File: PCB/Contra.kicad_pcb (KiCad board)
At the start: 2 copper layers, 251.5 x 76.2 mm, 152 parts, among them J1 Conn_01x03, J2 Conn_01x02, SW1 SW_PUSH, SW2 SW_SPDT, U1 ProMicro

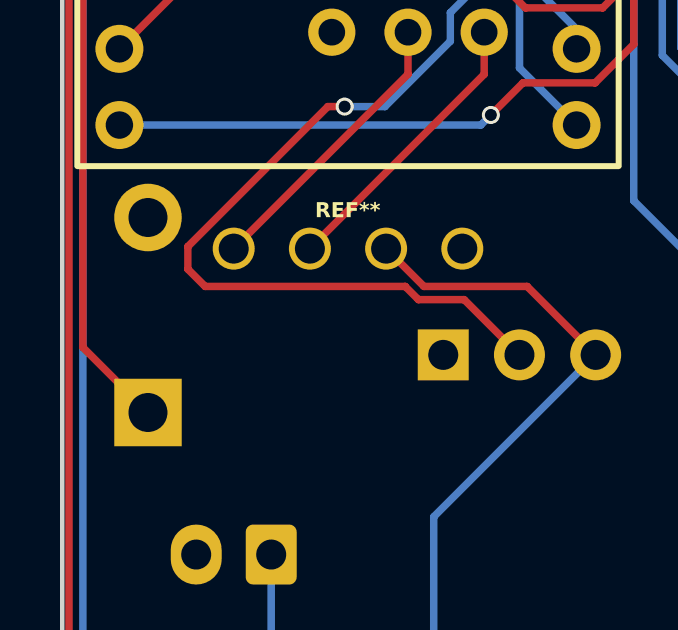
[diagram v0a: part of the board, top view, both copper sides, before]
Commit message: tweak reset switch location
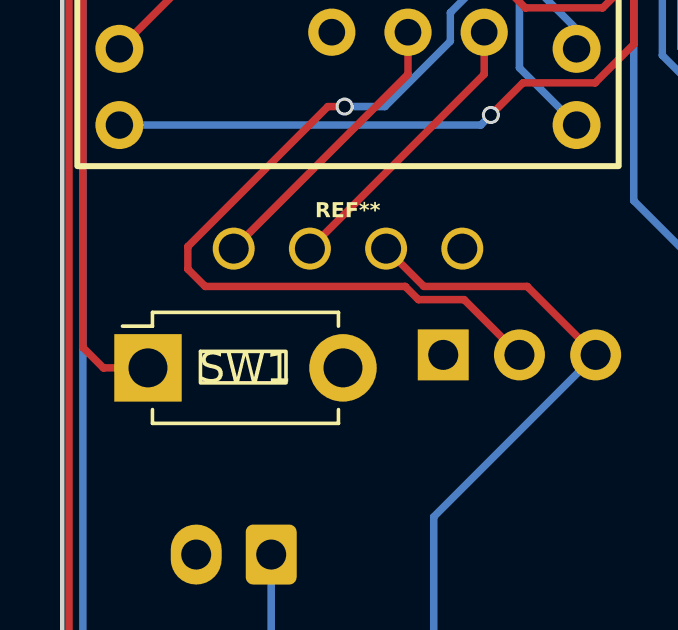
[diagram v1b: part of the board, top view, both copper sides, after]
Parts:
- SW1: moved to F.Cu
- moved SW1 1.49 mm to (26.7, 92.2), turned to 0 degrees
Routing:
- net Net-(U1-RST): track 33.8 -> 33.2 mm
